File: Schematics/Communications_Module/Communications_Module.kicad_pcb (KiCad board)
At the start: 4 copper layers, 69.5 x 60 mm, 72 parts, among them J1 USB_B_Micro, J2 SWD_01x04_Pin, J3 Stack Male Edge Connector, Q1 AO3400A, SW1 SW_STM_RESET, SW2 SW_STM_BOOT_MODE, U1 RFM95W-915S2, U2 W25Q128JVS, U3 AMS1117-3.3, U4 LM66100DCKR, U5 LM66100DCKR, U6 LM66100DCKR, U7 STM32F103CBT6, U8 ACS70331EOLC, U9 ISO1042BDWVR, Y1 X322516MMB4SI

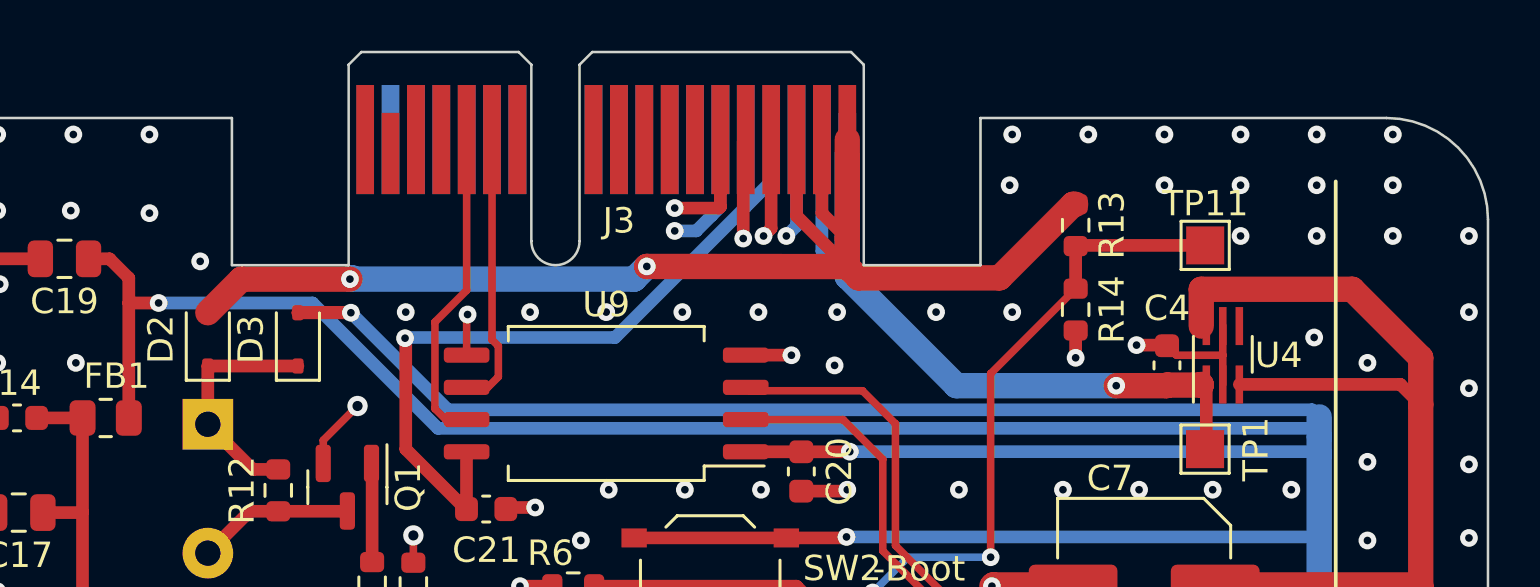
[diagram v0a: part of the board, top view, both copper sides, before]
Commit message: Updated layout to pass DRC with new copper-edge clearance
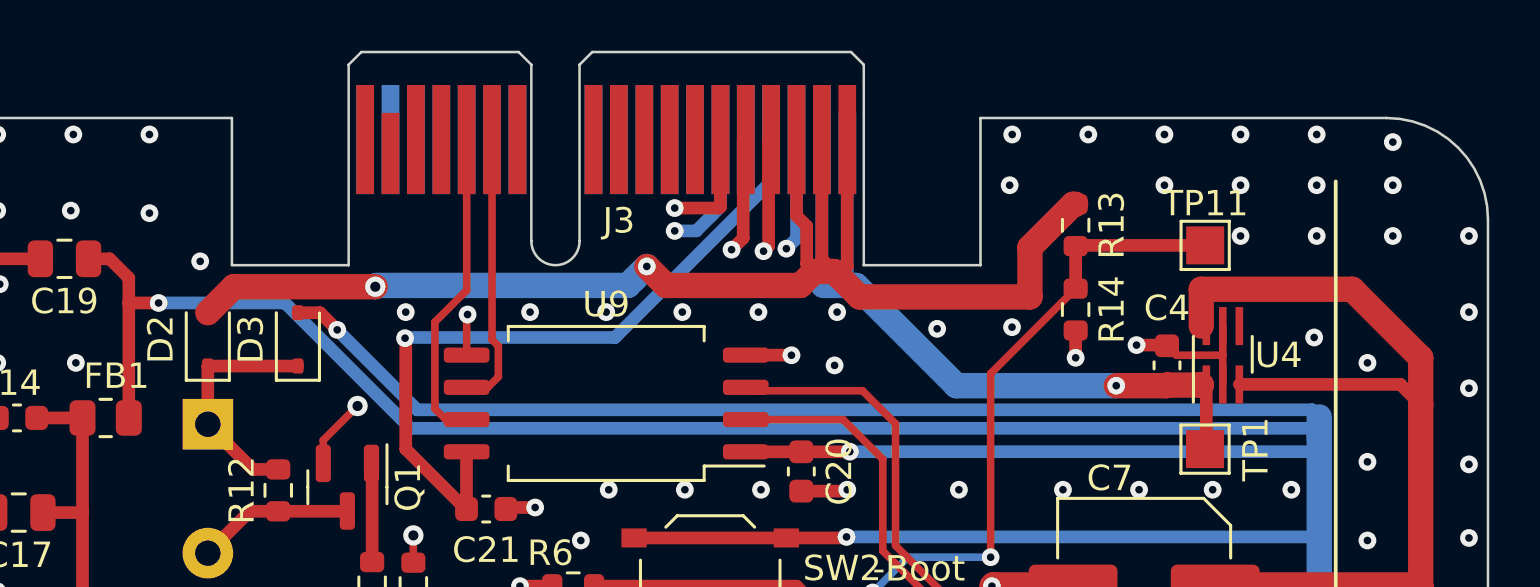
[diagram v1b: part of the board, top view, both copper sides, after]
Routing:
- net +BATT: track 51.6 -> 55.2 mm
- net +3.3V: track 531.8 -> 529.8 mm
- net GND: track 115.0 -> 116.6 mm
- net V_PSU: track 29.0 -> 30.2 mm

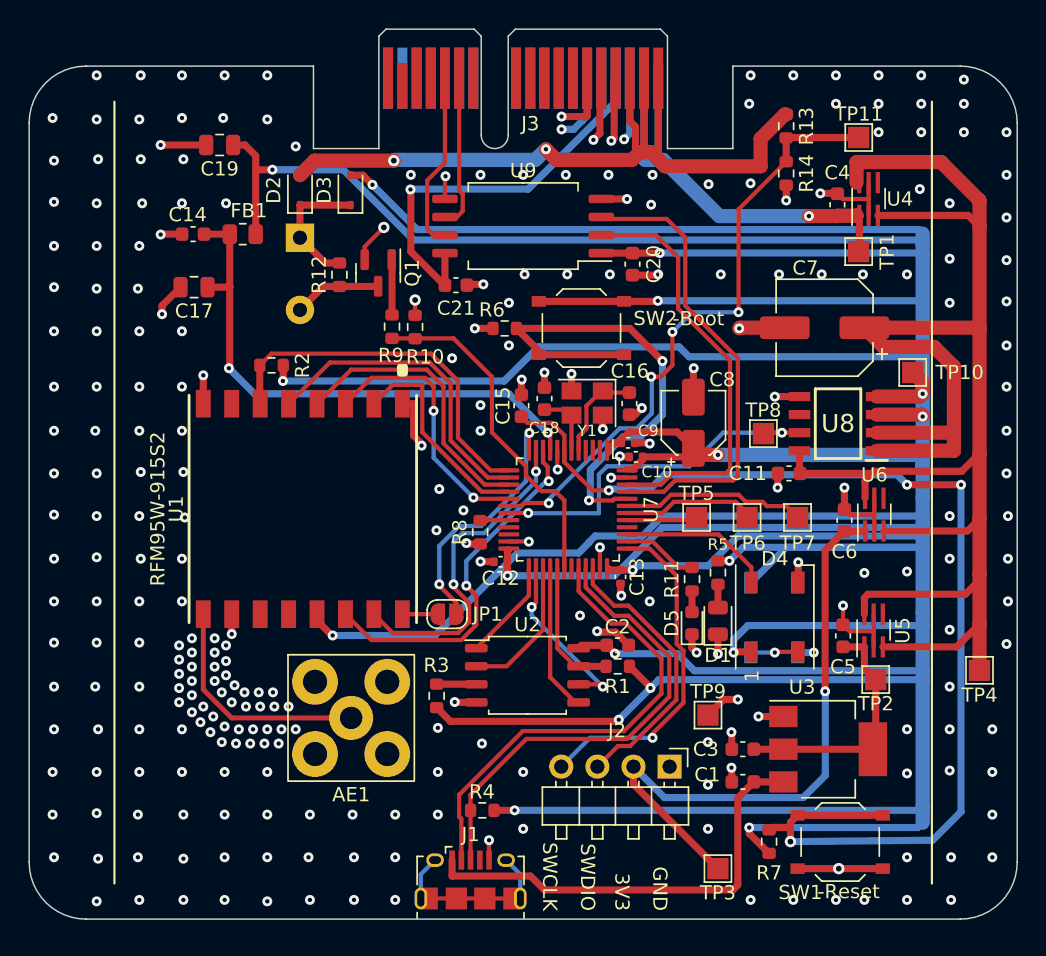
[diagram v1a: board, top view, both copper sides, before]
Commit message: Adjusted part nnumbers + ERC pass
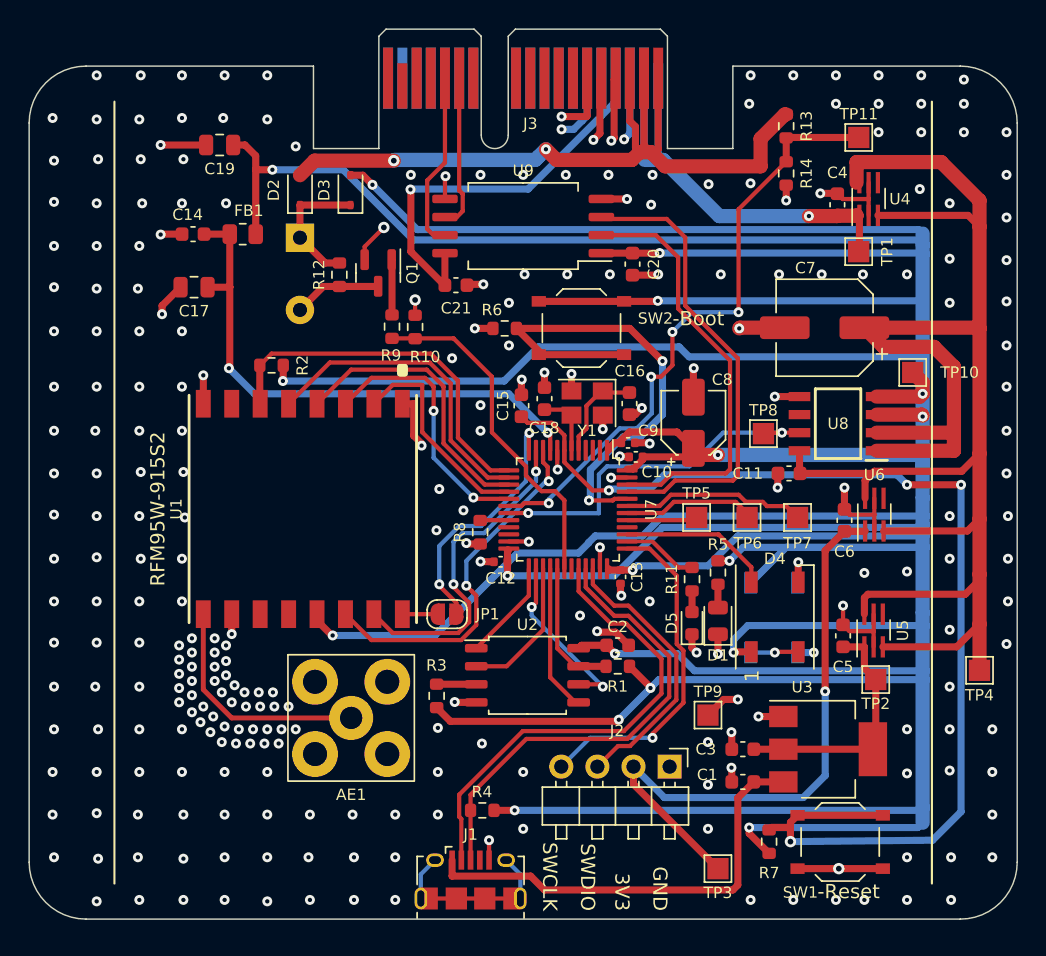
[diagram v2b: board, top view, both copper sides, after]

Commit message: Added type-C connector + tweaked PCB layout (DRC pass)
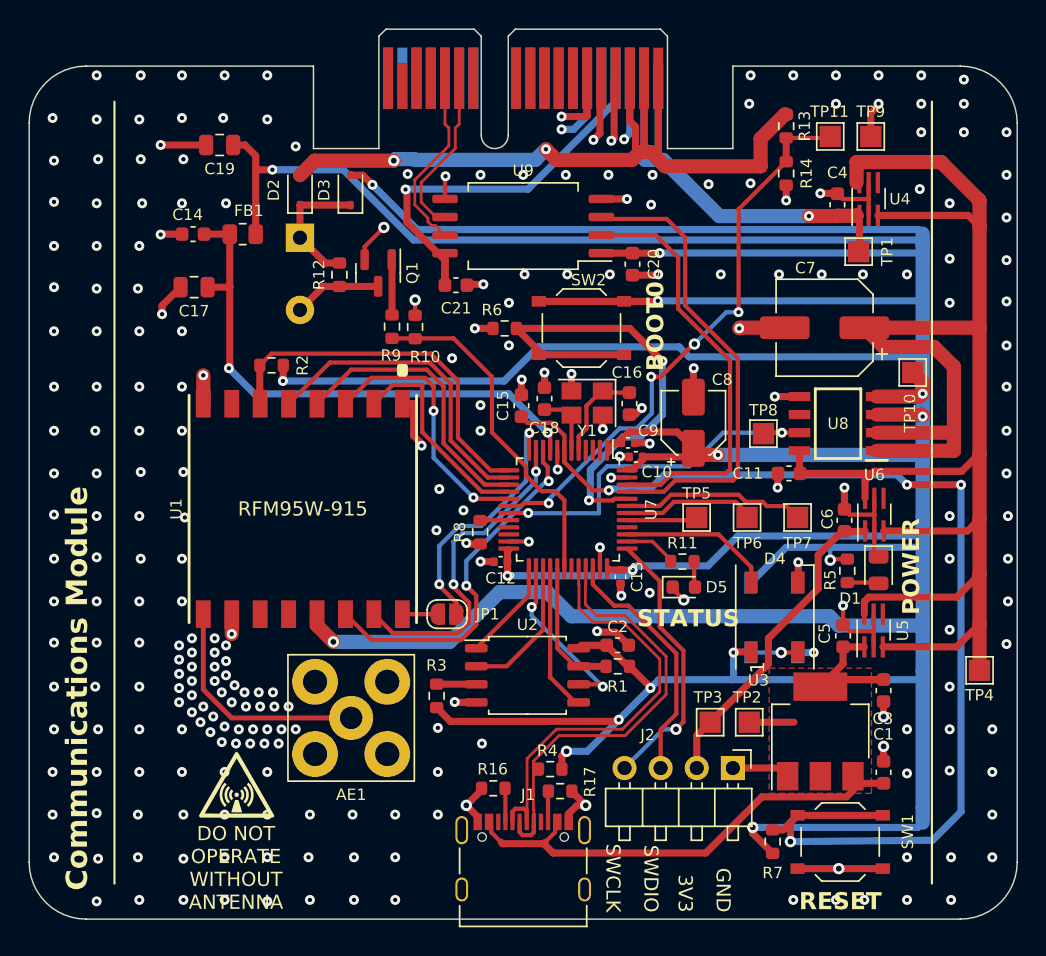
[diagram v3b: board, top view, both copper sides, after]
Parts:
- added R16: 5.1k, Resistor_SMD:R_0603_1608Metric, F.Cu at (136.9, 128.2)
- added R17: 5.1k, Resistor_SMD:R_0603_1608Metric, F.Cu at (141.6, 128.3)
- J1: value USB_B_Micro -> USB_C_Female_USB2_Small; footprint footprints:USB_Micro-B_Amphenol_10118194_Horizontal -> footprints:USB_C_DB-108PWB
- U1: value RFM95W-915S2 -> RFM95W-915
- moved TP9 42.3 mm to (163.4, 82.3)
- moved D1 11.9 mm to (164.0, 112.8), turned to -90 degrees
- moved C3 10.7 mm to (164.3, 121.3), turned to -90 degrees
- moved TP3 10.3 mm to (152.2, 123.5)
- moved C1 9.92 mm to (164.3, 127.0), turned to 90 degrees
- moved TP2 9.39 mm to (154.9, 123.5)
- moved R5 9.10 mm to (161.8, 112.8)
- moved R4 5.59 mm to (140.9, 126.8)
- moved J2 4.45 mm to (153.8, 126.7)
- moved J1 4.02 mm to (139.0, 133.0)
- moved D5 2.60 mm to (150.3, 114.0), turned to 0 degrees
- moved TP11 2.01 mm to (160.6, 82.3)
- moved R11 1.41 mm to (150.2, 112.2), turned to 180 degrees
- moved U3 1.37 mm to (159.9, 124.1), turned to 90 degrees
- moved R7 0.25 mm to (156.6, 131.9)
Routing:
- net +3.3V: track 529.8 -> 437.5 mm, vias 18 -> 17
- net V_SWD: track 43.9 -> 22.5 mm, vias 1 -> 0
- net unconnected-(J1-Shield-Pad6): track 13.2 -> 0.00 mm
- net GND: track 116.6 -> 123.2 mm, vias 281 -> 269
- net SWCLK: track 24.0 -> 19.3 mm
- net V_REGUSB: track 17.6 -> 13.1 mm
- net BATT_SENSE: track 43.7 -> 40.3 mm
- net USB_D-: track 33.7 -> 30.6 mm
- net USB_D+: track 33.5 -> 30.6 mm
- net /USB_5V: track 31.6 -> 33.9 mm
- net Net-(J1-CC1): track 0.00 -> 2.38 mm
- net SWDIO: track 19.7 -> 17.5 mm
- net Net-(J1-CC2): track 0.00 -> 2.18 mm
- net DB_LED: track 5.32 -> 3.72 mm
- net CAN_L: track 10.9 -> 11.9 mm
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- added copper zone on F.Cu, net V_REGUSB
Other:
- board text added: "BOOT0"
- board text added: "Communications Module"
- board text added: "DO NOT OPERATE WITHOUT ANTENNA"
- board text added: "POWER"
- board text added: "RESET"
- board text added: "STATUS"
- board text removed: "-Boot"
- board text removed: "-Reset"
- board text removed: "Boot Mode"
- board text removed: "Reset"

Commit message: PCB layout tweaks & Silkscreen added
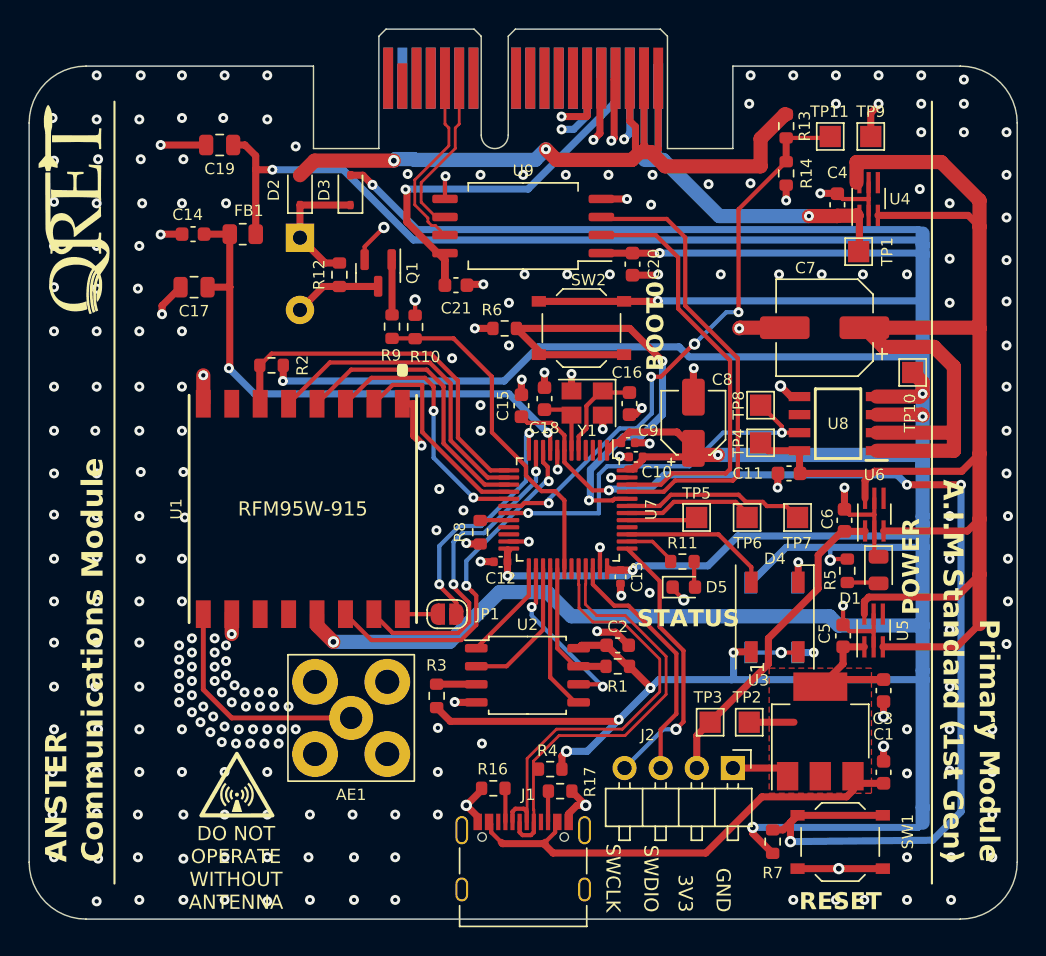
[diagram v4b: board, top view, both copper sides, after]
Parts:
- moved TP4 22.2 mm to (155.7, 103.8)
- moved TP8 2.01 mm to (155.7, 101.2)
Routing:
- net CURR_SENSE: track 25.7 -> 27.0 mm
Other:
- board text added: "A.I.M Standard (1st Gen)"
- board text added: "ANSTER"
- board text added: "Anster Rev 1.0 QRET Mar 2024 Oak Campbell Kennan Bays"
- board text added: "Primary Module"

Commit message: Fixed my horrendous via stitching precision
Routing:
- net V_MUX: track 125.1 -> 127.0 mm
- net GND: vias 269 -> 274

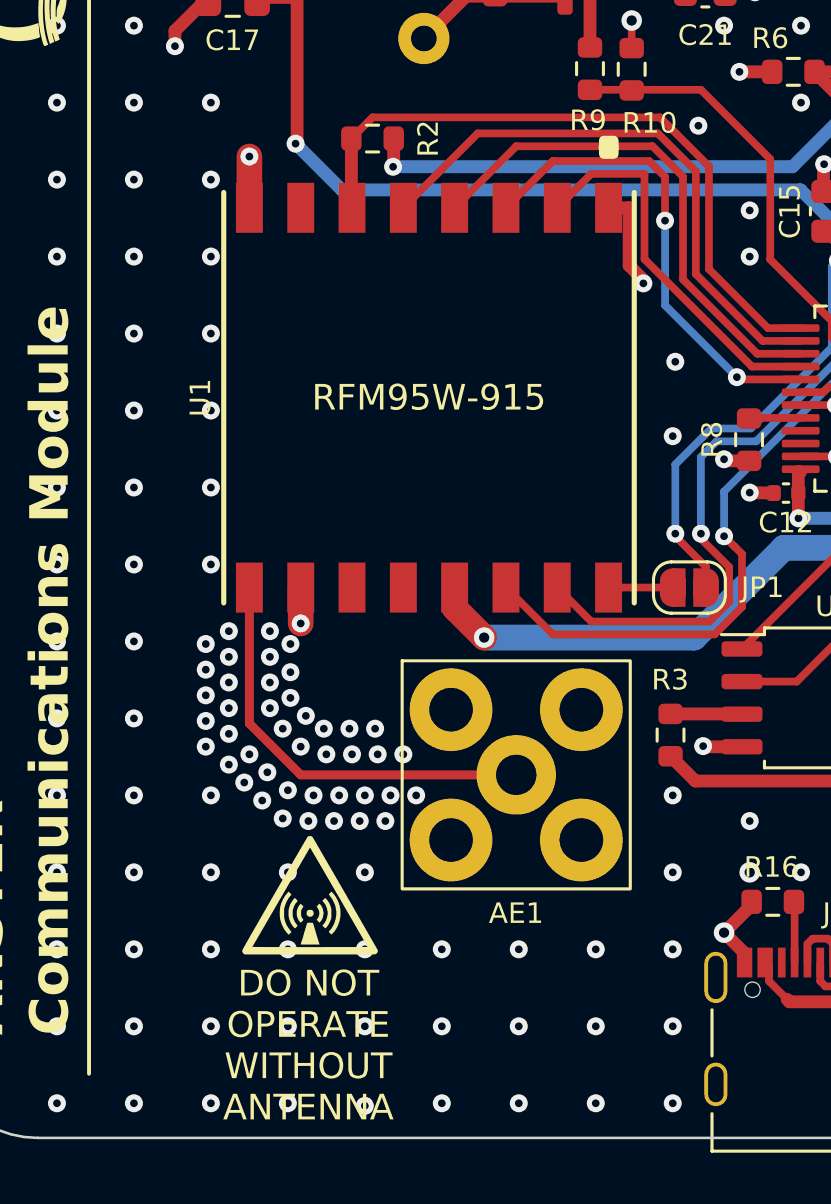
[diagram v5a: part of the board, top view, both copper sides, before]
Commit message: Change Debug & Power LED resistors
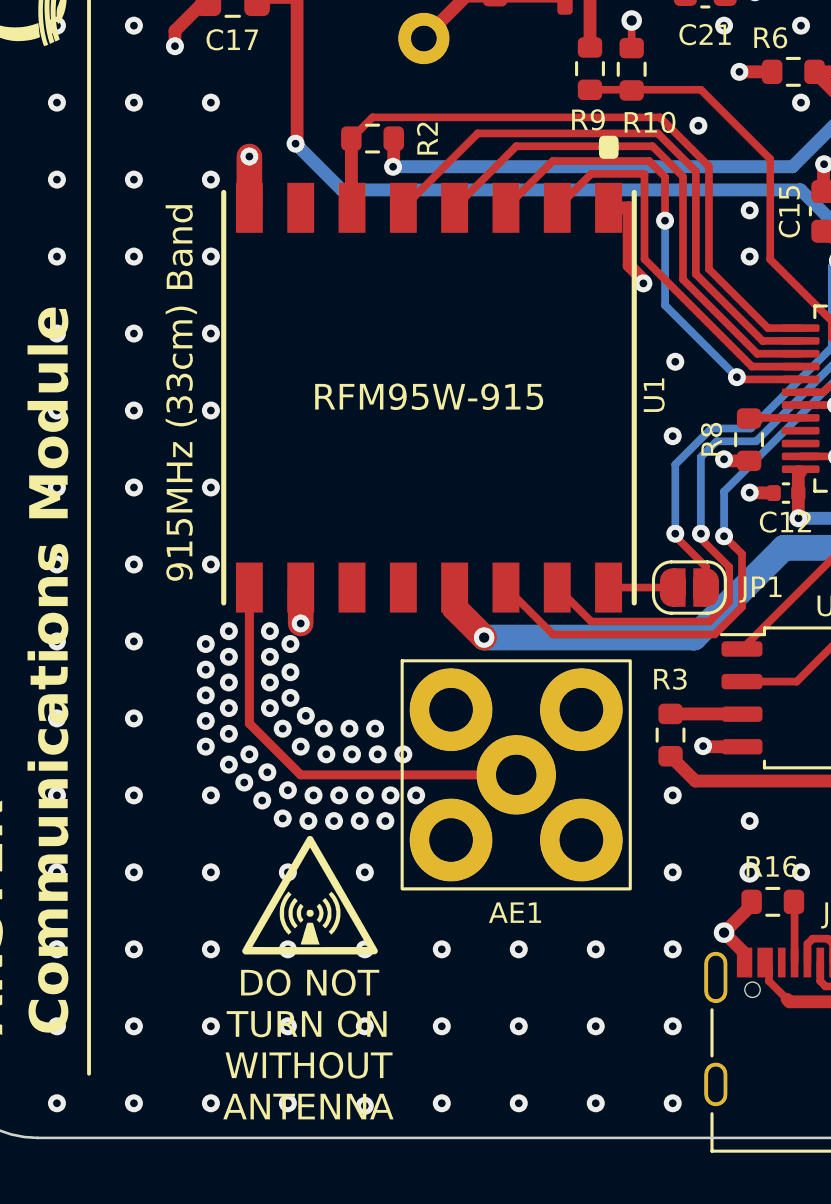
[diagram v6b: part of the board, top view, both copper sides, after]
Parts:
- R11: value 560R -> 680R
- R5: value 820R -> 1.2k
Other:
- board text added: "915MHz (33cm) Band"
- board text added: "DO NOT TURN ON WITHOUT ANTENNA"
- board text removed: "DO NOT OPERATE WITHOUT ANTENNA"
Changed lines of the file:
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@@
     (descr "Resistor SMD 0603 (1608 Metric), square (rectangular) end terminal, IPC_7351 nominal, (Body size source: IPC-SM-782 page 72, https://www.pcb-3d.com/wordpress/wp-content/uploads/ipc-sm-782a_amendment_1_and_2.pdf), generated with kicad-footprint-generator")
     (tags "resistor")
-    (property "LCSC" "C23253")
+    (property "LCSC" "C22765")
     (property "Sheetfile" "Communications_Module.kicad_sch")
     (property "Sheetname" "")
@@
         (effects (font (size 0.8 0.8) (thickness 0.1)))
     )
-    (fp_text value "820R" (at 0 1.43 90) (layer "F.Fab")
+    (fp_text value "1.2k" (at 0 1.43 90) (layer "F.Fab")
         (effects (font (size 1 1) (thickness 0.15)))
     )
@@
     (descr "Resistor SMD 0603 (1608 Metric), square (rectangular) end terminal, IPC_7351 nominal, (Body size source: IPC-SM-782 page 72, https://www.pcb-3d.com/wordpress/wp-content/uploads/ipc-sm-782a_amendment_1_and_2.pdf), generated with kicad-footprint-generator")
     (tags "resistor")
-    (property "LCSC" "C23204")
+    (property "LCSC" "C23228")
     (property "Sheetfile" "Communications_Module.kicad_sch")
     (property "Sheetname" "")
@@
         (effects (font (size 0.8 0.8) (thickness 0.1)))
     )
-    (fp_text value "560R" (at 0 1.43) (layer "F.Fab")
+    (fp_text value "680R" (at 0 1.43) (layer "F.Fab")
         (effects (font (size 1 1) (thickness 0.15)))
     )
@@
     (property "ki_keywords" "Low power long range transceiver module")
     (attr smd)
-    (fp_text reference "U1" (at 0 8.9 90) (layer "F.SilkS")
+    (fp_text reference "U1" (at -0.1 -8.8 90) (layer "F.SilkS")
         (effects (font (size 0.8 0.8) (thickness 0.1)))
     )
@@
     (effects (font (size 1.2 1.2) (thickness 0.2) bold) (justify left bottom))
   )
+  (gr_text "915MHz (33cm) Band" (at 114.4 108.3 90) (layer "F.SilkS")
+    (effects (font (size 1 1) (thickness 0.15)) (justify bottom))
+  )
   (gr_text "RESET" (at 158.4 136.8) (layer "F.SilkS" knockout)
     (effects (font (size 1.2 1.2) (thickness 0.2) bold) (justify left bottom))
   )
-  (gr_text "DO NOT\nOPERATE\nWITHOUT\nANTENNA" (at 118.8 136.751732) (layer "F.SilkS")
+  (gr_text "DO NOT\nTURN ON\nWITHOUT\nANTENNA" (at 118.8 136.751732) (layer "F.SilkS")
     (effects (font (size 1 1) (thickness 0.15)) (justify bottom))
   )
@@
     (polygon
       (pts
-        (xy 104.25 77.35)
-        (xy 173.75 77.35)
+        (xy 104.25 71.35)
+        (xy 173.75 71.35)
         (xy 173.75 137.35)
         (xy 104.25 137.35)
